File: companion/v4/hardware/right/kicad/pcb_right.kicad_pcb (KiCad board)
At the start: 2 copper layers, 40 x 20.2 mm, 17 parts, among them J1 TF31-6S-0.5SH_800_, J2 speaker, SW1 SW_Push, U1 113991254, U2 MAX98357AETE_T

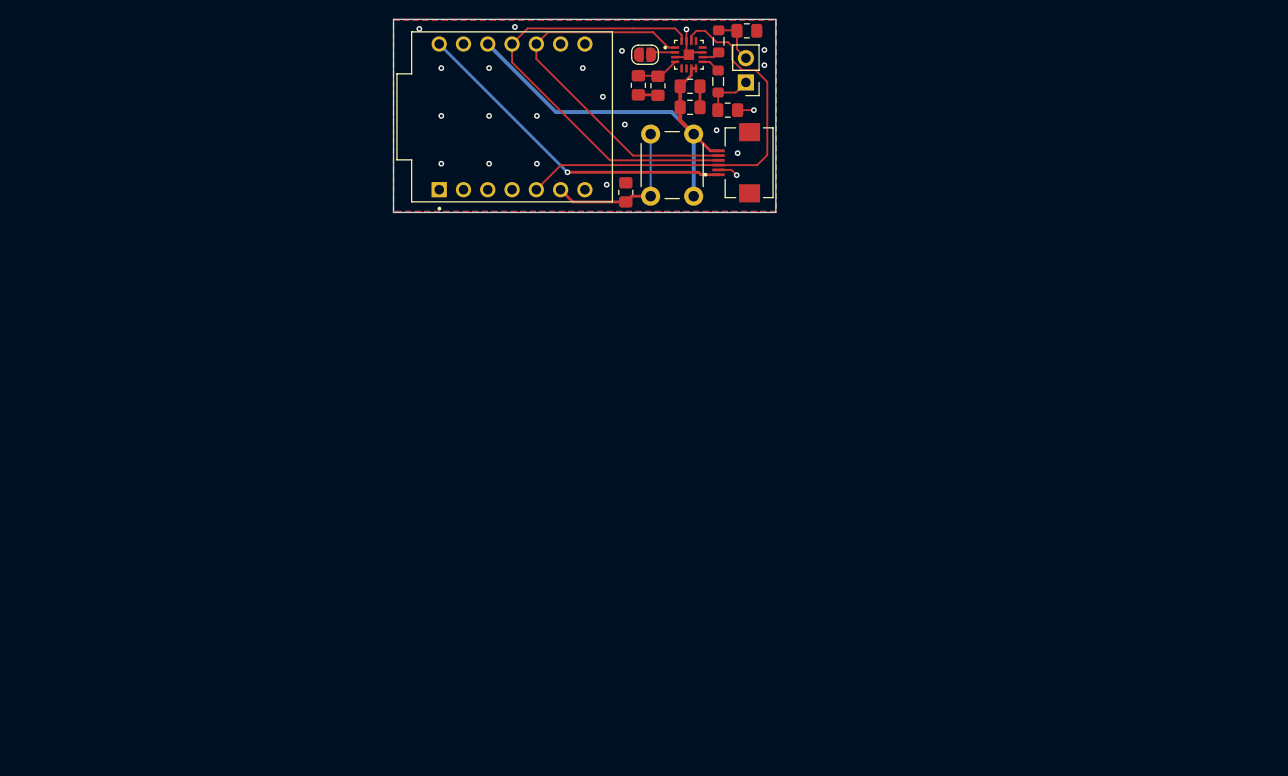
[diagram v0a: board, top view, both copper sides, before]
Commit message: addded component footprints
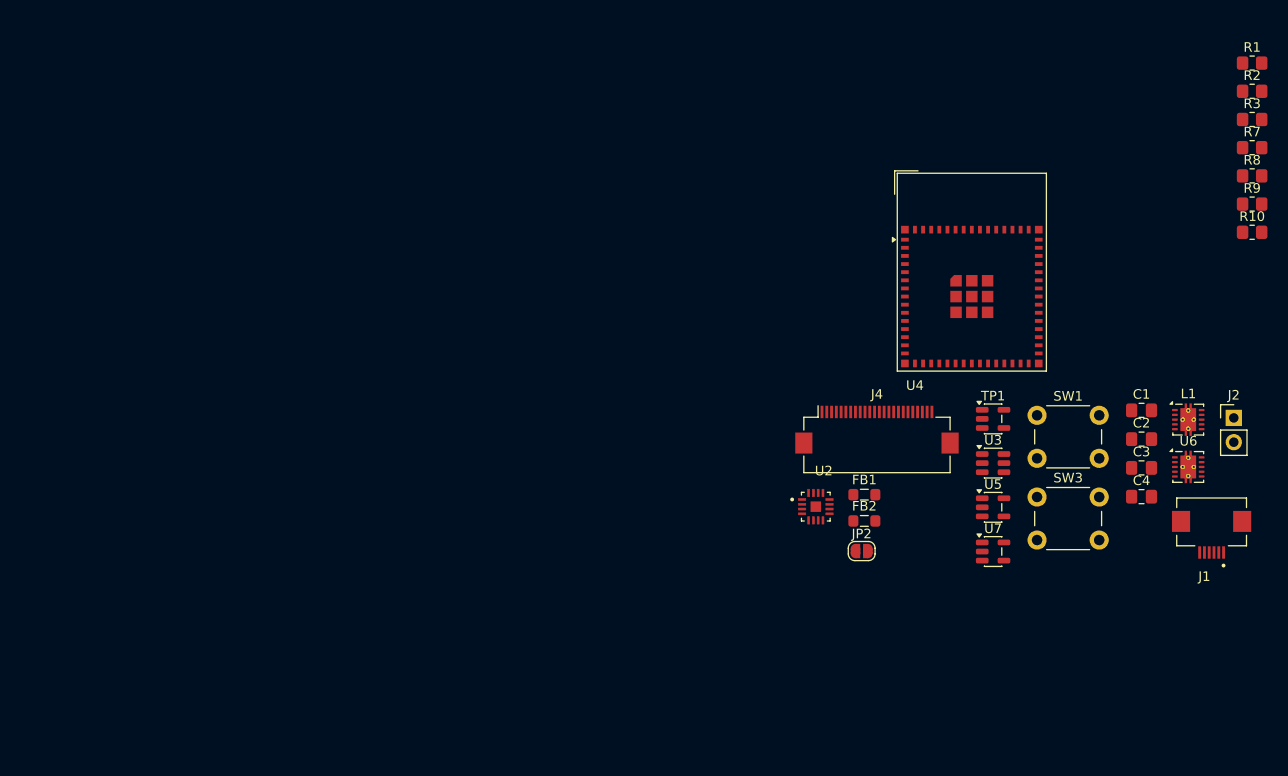
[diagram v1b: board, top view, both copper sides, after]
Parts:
- removed G***: LOGO, c6:logo1
- removed G***: LOGO, c6:neu
- removed U1: 113991254, c6:MODULE_113991254
- added J4: Conn_01x24_MountingPin, Connector_FFC-FPC:Hirose_FH12-24S-0.5SH_1x24-1MP_P0.50mm_Horizontal, F.Cu at (150.6, 92.8)
- added L1: 2.2uH, Package_SON:Texas_DRC0010J_ThermalVias, F.Cu at (183.1, 91.8)
- added R10: 10k, Resistor_SMD:R_0805_2012Metric_Pad1.20x1.40mm_HandSolder, F.Cu at (189.8, 72.2)
- added R7: 4.7k, Resistor_SMD:R_0805_2012Metric_Pad1.20x1.40mm_HandSolder, F.Cu at (189.8, 63.3)
- added R8: 4.7k, Resistor_SMD:R_0805_2012Metric_Pad1.20x1.40mm_HandSolder, F.Cu at (189.8, 66.3)
- added R9: 10k, Resistor_SMD:R_0805_2012Metric_Pad1.20x1.40mm_HandSolder, F.Cu at (189.8, 69.2)
- added SW3: SW_RESET, Button_Switch_THT:SW_PUSH_6mm_H5mm, F.Cu at (167.3, 99.9)
- added TP1: TX, Package_TO_SOT_SMD:SOT-23-5, F.Cu at (162.7, 91.7)
- added U3: USBLC6-2SC6, Package_TO_SOT_SMD:SOT-23-6, F.Cu at (162.7, 96.3)
- added U4: ESP32-S3-MINI-1, RF_Module:ESP32-S2-MINI-1, F.Cu at (160.5, 76.3)
- added U5: TLV75528PDBV, Package_TO_SOT_SMD:SOT-23-5, F.Cu at (162.7, 101.0)
- added U6: TPS63001, Package_SON:Texas_DRC0010J_ThermalVias, F.Cu at (183.1, 96.7)
- added U7: TLV75515PDBV, Package_TO_SOT_SMD:SOT-23-5, F.Cu at (162.7, 105.6)
- R1: value 47k -> 100k
- R3: value 100k -> 100
- SW1: value SW_Push -> SW_BOOT
- moved R3 66.0 mm to (189.8, 60.4), turned to 0 degrees
- moved R2 64.2 mm to (189.8, 57.4), turned to 0 degrees
- moved C4 63.8 mm to (178.3, 99.8)
- moved R1 62.2 mm to (189.8, 54.5), turned to 0 degrees
- moved J2 61.9 mm to (187.9, 91.6), turned to 0 degrees
- moved J1 61.3 mm to (185.6, 102.5), turned to 0 degrees
- moved C3 60.4 mm to (178.3, 96.8)
- moved C2 59.4 mm to (178.3, 93.8), turned to 0 degrees
- moved JP2 56.7 mm to (149.0, 105.5)
- moved C1 53.5 mm to (178.3, 90.8)
- moved FB1 49.8 mm to (149.3, 99.6), turned to 0 degrees
- moved U2 49.1 mm to (144.2, 100.9)
- moved FB2 48.5 mm to (149.3, 102.4), turned to 0 degrees
- moved SW1 46.5 mm to (167.3, 91.3), turned to 0 degrees
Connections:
- R1 pad 2: GND -> +3.3V
- R3 pad 1: Net-(U1-D5) -> +5V
- R3 pad 2: GND -> Net-(U6-EN)
- SW1 pad 1: Net-(U1-D5) -> GND
- SW1 pad 2: +3.3V -> Net-(U4-IO0)
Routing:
- net BCLK: track 47.1 -> 0.00 mm
- net LRCLK: track 45.1 -> 0.00 mm
- net +3.3V: track 43.7 -> 0.00 mm
- net DIN: track 40.5 -> 0.00 mm
- net +5V: track 34.9 -> 0.00 mm, vias 1 -> 0
- net Net-(U1-D5): track 16.7 -> 0.00 mm
- net GND: track 13.9 -> 0.00 mm, vias 22 -> 0
- net Net-(J2-Pin_1): track 5.20 -> 0.00 mm
- net Net-(J2-Pin_2): track 5.18 -> 0.00 mm
- net Net-(U2-SD_MODE): track 4.89 -> 0.00 mm
- net Net-(JP2-B): track 2.60 -> 0.00 mm
- net Net-(U2-OUTP): track 2.00 -> 0.00 mm
- net Net-(U2-OUTN): track 1.89 -> 0.00 mm
- removed copper zone on B.Cu, net GND
- removed copper zone on F.Cu, net GND
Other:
- board outline removed
- board text removed: "AI GLASSES V3"
- board text removed: "SINRG LAB"

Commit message: started layout
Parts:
- added C10: 1u, Capacitor_SMD:C_0402_1005Metric, F.Cu at (161.5, 102.7)
- added C11: 1uf, Capacitor_SMD:C_0402_1005Metric, F.Cu at (161.5, 104.7)
- added C12: 1uf, Capacitor_SMD:C_0402_1005Metric, F.Cu at (161.5, 106.7)
- added C13: 100n, Capacitor_SMD:C_0402_1005Metric, F.Cu at (161.5, 108.6)
- added C14: 1uf, Capacitor_SMD:C_0402_1005Metric, F.Cu at (161.5, 110.6)
- added C15: 1uf, Capacitor_SMD:C_0402_1005Metric, F.Cu at (164.4, 98.8)
- added C16: 100n, Capacitor_SMD:C_0402_1005Metric, F.Cu at (164.4, 100.8)
- added C17: 1uf, Capacitor_SMD:C_0402_1005Metric, F.Cu at (164.4, 102.7)
- added C18: 100nf, Capacitor_SMD:C_0402_1005Metric, F.Cu at (164.4, 104.7)
- added C19: 1uf, Capacitor_SMD:C_0402_1005Metric, F.Cu at (164.4, 106.7)
- added C20: 100nf, Capacitor_SMD:C_0402_1005Metric, F.Cu at (164.4, 108.6)
- added C21: 1uf, Capacitor_SMD:C_0402_1005Metric, F.Cu at (164.4, 110.6)
- added C22: 100nf, Capacitor_SMD:C_0402_1005Metric, F.Cu at (167.2, 98.8)
- added C23: 47uf, Capacitor_SMD:C_0402_1005Metric, F.Cu at (167.2, 100.8)
- added C24: 10uf, Capacitor_SMD:C_0402_1005Metric, F.Cu at (167.2, 102.7)
- added C25: 0.1uf, Capacitor_SMD:C_0402_1005Metric, F.Cu at (167.2, 104.7)
- added C26: 10uf, Capacitor_SMD:C_0402_1005Metric, F.Cu at (167.2, 106.7)
- added C27: 10uf, Capacitor_SMD:C_0402_1005Metric, F.Cu at (167.2, 108.6)
- added C28: 0.1uf, Capacitor_SMD:C_0402_1005Metric, F.Cu at (167.2, 110.6)
- added C8: 10uf, Capacitor_SMD:C_0402_1005Metric, F.Cu at (161.5, 98.8)
- added C9: 0.1uf, Capacitor_SMD:C_0402_1005Metric, F.Cu at (161.5, 100.8)
- added J3: USB_C_Receptacle_USB2.0_14P, Connector_USB:USB_C_Receptacle_HRO_TYPE-C-31-M-12, F.Cu at (126.3, 112.5)
- added R11: 10kΩ, Resistor_SMD:R_0402_1005Metric, F.Cu at (173.2, 87.6)
- added R4: 10kΩ, Resistor_SMD:R_0402_1005Metric, F.Cu at (173.2, 81.6)
- added R5: 5.1kΩ, Resistor_SMD:R_0402_1005Metric, F.Cu at (173.2, 83.6)
- added R6: 5.1kΩ, Resistor_SMD:R_0402_1005Metric, F.Cu at (173.2, 85.6)
- added TP2: RX, TestPoint:TestPoint_Pad_D1.5mm, F.Cu at (173.5, 75.3)
- added TP3: GND, TestPoint:TestPoint_Pad_D1.5mm, F.Cu at (173.5, 78.9)
- moved U4 97.9 mm to (71.5, 117.2), turned to 90 degrees
- moved J1 83.6 mm to (104.3, 122.0), turned to -90 degrees
- moved J4 68.3 mm to (86.8, 117.3), turned to 90 degrees
- moved J2 34.9 mm to (157.4, 108.6)
- moved U6 34.9 mm to (152.7, 113.8)
- moved L1 34.9 mm to (152.7, 108.8)
- moved C1 29.2 mm to (169.4, 63.0)
- moved C2 29.2 mm to (169.4, 66.0)
- moved C3 29.2 mm to (169.4, 69.0)
- moved C4 29.2 mm to (169.4, 72.0)
- moved R10 29.0 mm to (169.3, 92.7)
- moved R2 29.0 mm to (169.3, 78.0)
- moved R3 29.0 mm to (169.3, 80.9)
- moved R9 29.0 mm to (169.3, 89.8)
- moved R1 29.0 mm to (169.3, 75.0)
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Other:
- board outline added: 44.5 x 19 mm
